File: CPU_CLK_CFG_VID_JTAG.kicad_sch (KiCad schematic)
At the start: 1 part

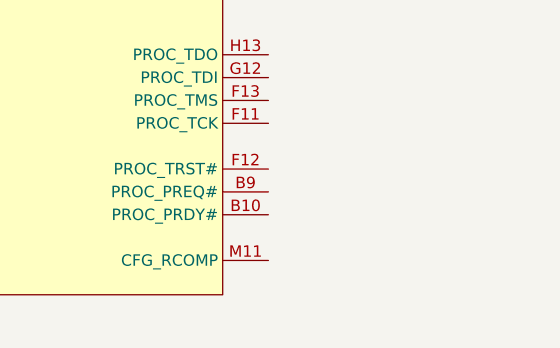
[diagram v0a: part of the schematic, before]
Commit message: partially added eDP + rearranged other display stuff
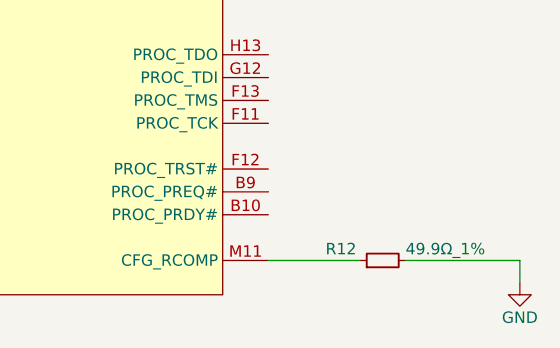
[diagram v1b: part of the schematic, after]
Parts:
- added R12: 49.9Ω_1%, Resistor_SMD:R_0402_1005Metric, symbol Device:R_Small
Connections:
- net at JCPU1.M11 (CFG_RCOMP): now also R12.1
- new net GND: R12.2
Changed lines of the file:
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@@
+	(wire
+		(pts
+			(xy 200.66 138.43) (xy 187.96 138.43)
+		)
+		(stroke
+			(width 0)
+			(type default)
+		)
+	)
 	(wire
 		(pts
@@
 	(wire
 		(pts
+			(xy 182.88 138.43) (xy 172.72 138.43)
+		)
+		(stroke
+			(width 0)
+			(type default)
+		)
+	)
+	(wire
+		(pts
+			(xy 200.66 138.43) (xy 200.66 140.97)
+		)
+		(stroke
+			(width 0)
+			(type default)
+		)
+	)
+	(wire
+		(pts
 			(xy 106.68 52.07) (xy 111.76 52.07)
 		)
@@
 			)
 		)
+	)
+	(symbol
+		(lib_id "Device:R_Small")
+		(at 185.42 138.43 90)
+		(unit 1)
+		(exclude_from_sim no)
+		(in_bom yes)
+		(on_board yes)
+		(dnp no)
+		(property "Reference" "R12"
+			(at 179.07 137.16 90)
+			(effects
+				(font
+					(size 1.27 1.27)
+				)
+				(justify right)
+			)
+		)
+		(property "Value" "49.9Ω_1%"
+			(at 187.96 137.16 90)
+			(effects
+				(font
+					(size 1.27 1.27)
+				)
+				(justify right)
+			)
+		)
+		(property "Footprint" "Resistor_SMD:R_0402_1005Metric"
+			(at 185.42 138.43 0)
+			(effects
+				(font
+					(size 1.27 1.27)
+				)
+				(hide yes)
+			)
+		)
+		(property "Datasheet" "~"
+			(at 185.42 138.43 0)
+			(effects
+				(font
+					(size 1.27 1.27)
+				)
+				(hide yes)
+			)
+		)
+		(property "Description" "Resistor, small symbol"
+			(at 185.42 138.43 0)
+			(effects
+				(font
+					(size 1.27 1.27)
+				)
+				(hide yes)
+			)
+		)
+		(pin "1"
+		)
+		(pin "2"
+		)
+		(instances
+			(project "Stroopwafel-LGA1151-CFL"
+				(path "/4bc771b8-eb19-46d0-8798-27231a7c6e83/1c68e8a0-095a-4b5e-9e5b-76592d9951b4"
+					(reference "R12")
+					(unit 1)
+				)
+			)
+		)
+	)
+	(symbol
+		(lib_id "power:GND")
+		(at 200.66 140.97 0)
+		(unit 1)
+		(exclude_from_sim no)
+		(in_bom yes)
+		(on_board yes)
+		(dnp no)
+		(property "Reference" "#PWR034"
+			(at 200.66 147.32 0)
+			(effects
+				(font
+					(size 1.27 1.27)
+				)
+				(hide yes)
+			)
+		)
+		(property "Value" "GND"
+			(at 200.66 144.78 0)
+			(effects
+				(font
+					(size 1.27 1.27)
+				)
+			)
+		)
+		(property "Footprint" ""
+			(at 200.66 140.97 0)
+			(effects
+				(font
+					(size 1.27 1.27)
+				)
+				(hide yes)
+			)
+		)
+		(property "Datasheet" ""
+			(at 200.66 140.97 0)
+			(effects
+				(font
+					(size 1.27 1.27)
+				)
+				(hide yes)
+			)
+		)
+		(property "Description" "Power symbol creates a global label with name \"GND\" , ground"
+			(at 200.66 140.97 0)
+			(effects
+				(font
+					(size 1.27 1.27)
+				)
+				(hide yes)
+			)
+		)
+		(pin "1"
+		)
+		(instances
+			(project "Stroopwafel-LGA1151-CFL"
+				(path "/4bc771b8-eb19-46d0-8798-27231a7c6e83/1c68e8a0-095a-4b5e-9e5b-76592d9951b4"
+					(reference "#PWR034")
+					(unit 1)
+				)
+			)
+		)

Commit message: Added LGA1151 socket bracket holes
stolen from another lga1151 footprint that has wrong pin numbers....
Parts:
- JCPU1: footprint A-my-stuff:LGA-1151_L47.1-W42.5-P0.91_PE115127-4041-01H -> A-my-stuff:LGA1151_TE-2287402-1
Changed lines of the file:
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@@
 			)
 		)
-		(property "Footprint" "A-my-stuff:LGA-1151_L47.1-W42.5-P0.91_PE115127-4041-01H"
+		(property "Footprint" "A-my-stuff:LGA1151_TE-2287402-1"
 			(at 142.24 246.38 0)
 			(effects

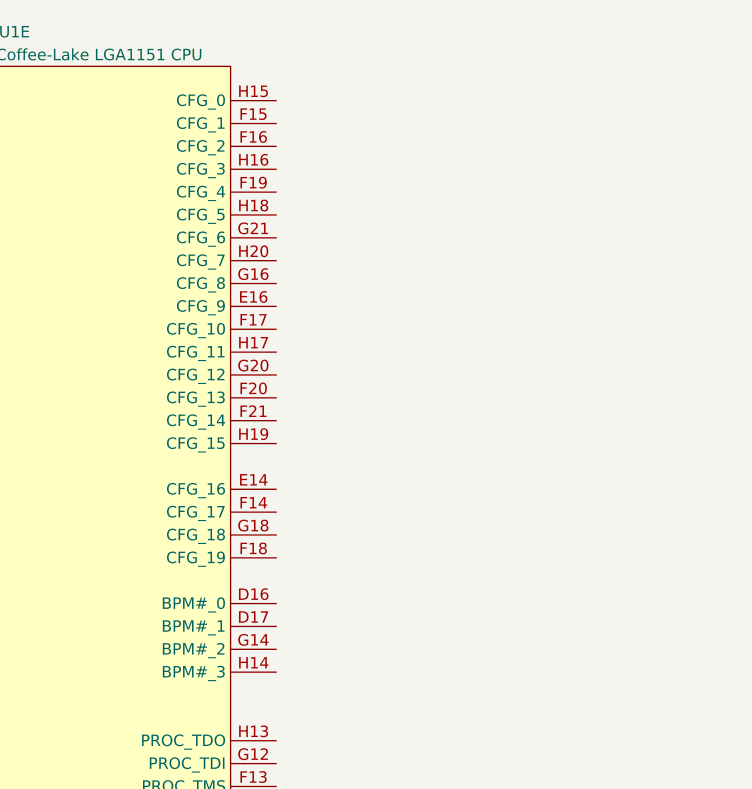
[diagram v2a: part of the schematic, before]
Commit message: Added CPU CFG resistors
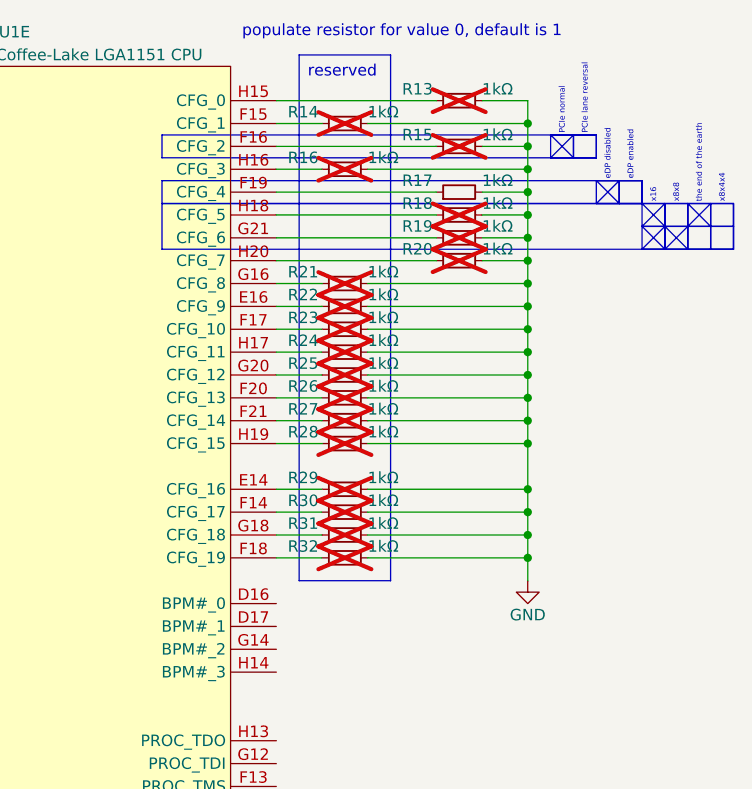
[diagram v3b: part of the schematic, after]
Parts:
- added R13, R14, R15, R16, R17, R18, R19, R20, R21, R22, R23, R24, R25, R26, R27, R28, R29, R30, R31, R32: 1kΩ, Resistor_SMD:R_0402_1005Metric, symbol Device:R_Small
- JCPU1: footprint A-my-stuff:LGA1151_TE-2287402-1 -> A-my-stuff:LGA-1151_L47.1-W42.5-P0.91_PE115127-4041-01H
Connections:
- net GND: now also R13.2, R14.2, R15.2, R16.2, R17.2, R18.2, R19.2, R20.2, R21.2, R22.2, R23.2, R24.2, R25.2, R26.2, R27.2, R28.2, R29.2, R30.2, R31.2, R32.2
- net at JCPU1.E14 (CFG_16): now also R29.1
- net at JCPU1.E16 (CFG_9): now also R22.1
- net at JCPU1.F14 (CFG_17): now also R30.1
- net at JCPU1.F15 (CFG_1): now also R14.1
- net at JCPU1.F16 (CFG_2): now also R15.1
- net at JCPU1.F17 (CFG_10): now also R23.1
- net at JCPU1.F18 (CFG_19): now also R32.1
- net at JCPU1.F19 (CFG_4): now also R17.1
- net at JCPU1.F20 (CFG_13): now also R26.1
- net at JCPU1.F21 (CFG_14): now also R27.1
- net at JCPU1.G16 (CFG_8): now also R21.1
- net at JCPU1.G18 (CFG_18): now also R31.1
- net at JCPU1.G20 (CFG_12): now also R25.1
- net at JCPU1.G21 (CFG_6): now also R19.1
- net at JCPU1.H15 (CFG_0): now also R13.1
- net at JCPU1.H16 (CFG_3): now also R16.1
- net at JCPU1.H17 (CFG_11): now also R24.1
- net at JCPU1.H18 (CFG_5): now also R18.1
- net at JCPU1.H19 (CFG_15): now also R28.1
- net at JCPU1.H20 (CFG_7): now also R20.1
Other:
- note added: "PCIe lane reversal"
- note added: "PCIe normal"
- note added: "eDP disabled"
- note added: "eDP enabled"
- note added: "populate resistor for value 0, default is 1"
- note added: "the end of the earth"
- note added: "x16"
- note added: "x8x4x4"
- note added: "x8x8"

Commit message: stroopwafel.exe
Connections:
- net CPU_24MCLK+: no longer JCPU1.K9 (CLK24P)
- net CPU_24MCLK-: no longer JCPU1.J9 (CLK24N)
- net CPU_BCLK+: no longer JCPU1.W5 (BCLKP)
- net CPU_BCLK-: no longer JCPU1.W4 (BCLKN)
- net CPU_PCIBCLK+: no longer JCPU1.W1 (PCI_BCLKP)
- net CPU_PCIBCLK-: no longer JCPU1.W2 (PCI_BCLKN)
- net at R30.1: no longer JCPU1.F14 (CFG_17)
- net at R12.1: no longer JCPU1.M11 (CFG_RCOMP)
- net at R29.1: no longer JCPU1.E14 (CFG_16)
- net at R20.1: no longer JCPU1.H20 (CFG_7)
- net at R27.1: no longer JCPU1.F21 (CFG_14)
- net at R24.1: no longer JCPU1.H17 (CFG_11)
- net at R14.1: no longer JCPU1.F15 (CFG_1)
- net at R25.1: no longer JCPU1.G20 (CFG_12)
- net at R23.1: no longer JCPU1.F17 (CFG_10)
- net at R28.1: no longer JCPU1.H19 (CFG_15)
- net at R15.1: no longer JCPU1.F16 (CFG_2)
- net at R13.1: no longer JCPU1.H15 (CFG_0)
- net at R19.1: no longer JCPU1.G21 (CFG_6)
- net at R31.1: no longer JCPU1.G18 (CFG_18)
- net at R16.1: no longer JCPU1.H16 (CFG_3)
- net at R32.1: no longer JCPU1.F18 (CFG_19)
- net at R17.1: no longer JCPU1.F19 (CFG_4)
- net at R22.1: no longer JCPU1.E16 (CFG_9)
- net at R21.1: no longer JCPU1.G16 (CFG_8)
- net at R26.1: no longer JCPU1.F20 (CFG_13)
- net at R18.1: no longer JCPU1.H18 (CFG_5)
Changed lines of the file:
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@@
 		(lib_id "A-my-stuff:Intel_CFL_1151")
 		(at 142.24 134.62 0)
-		(unit 5)
+		(unit 1)
 		(exclude_from_sim no)
 		(in_bom yes)
@@
 		(pin "J5"
 		)
-		(instances
-			(project ""
-				(path "/4bc771b8-eb19-46d0-8798-27231a7c6e83/061fe2d6-87c2-48c2-90bb-0928700512fc"
-					(reference "JCPU1")
-					(unit 5)
-				)
-				(path "/4bc771b8-eb19-46d0-8798-27231a7c6e83/1c68e8a0-095a-4b5e-9e5b-76592d9951b4"
-					(reference "JCPU1")
-					(unit 5)
-				)
-			)
-		)
 	)

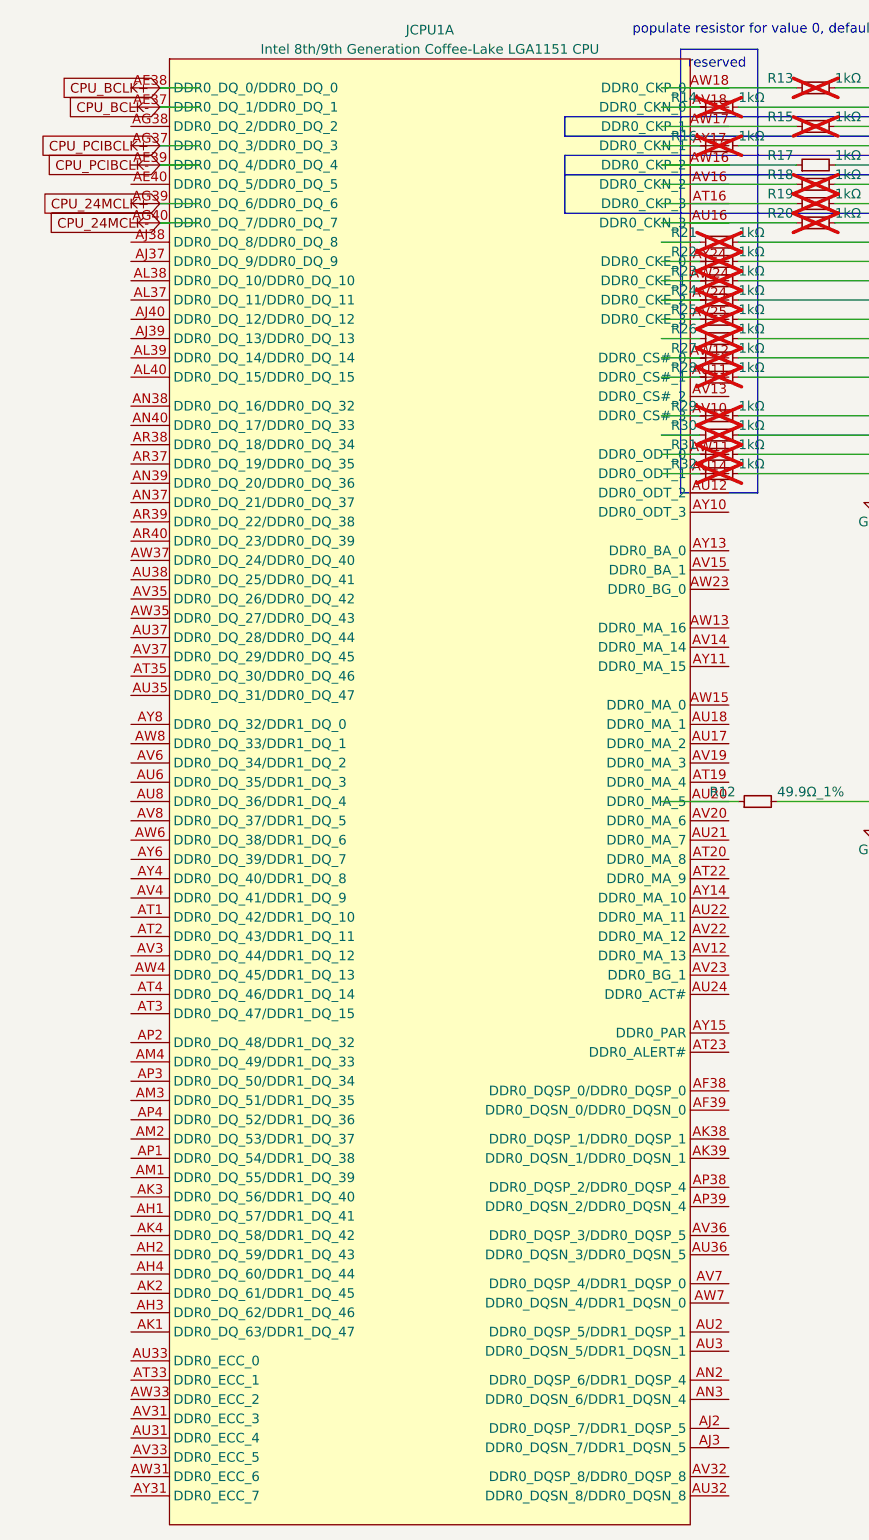
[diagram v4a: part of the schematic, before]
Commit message: Fixed entire schematic being broken
somehow every symbol with index 1 broke and updating the pcb stopped working. how does that even happen. oh well it's fixed now
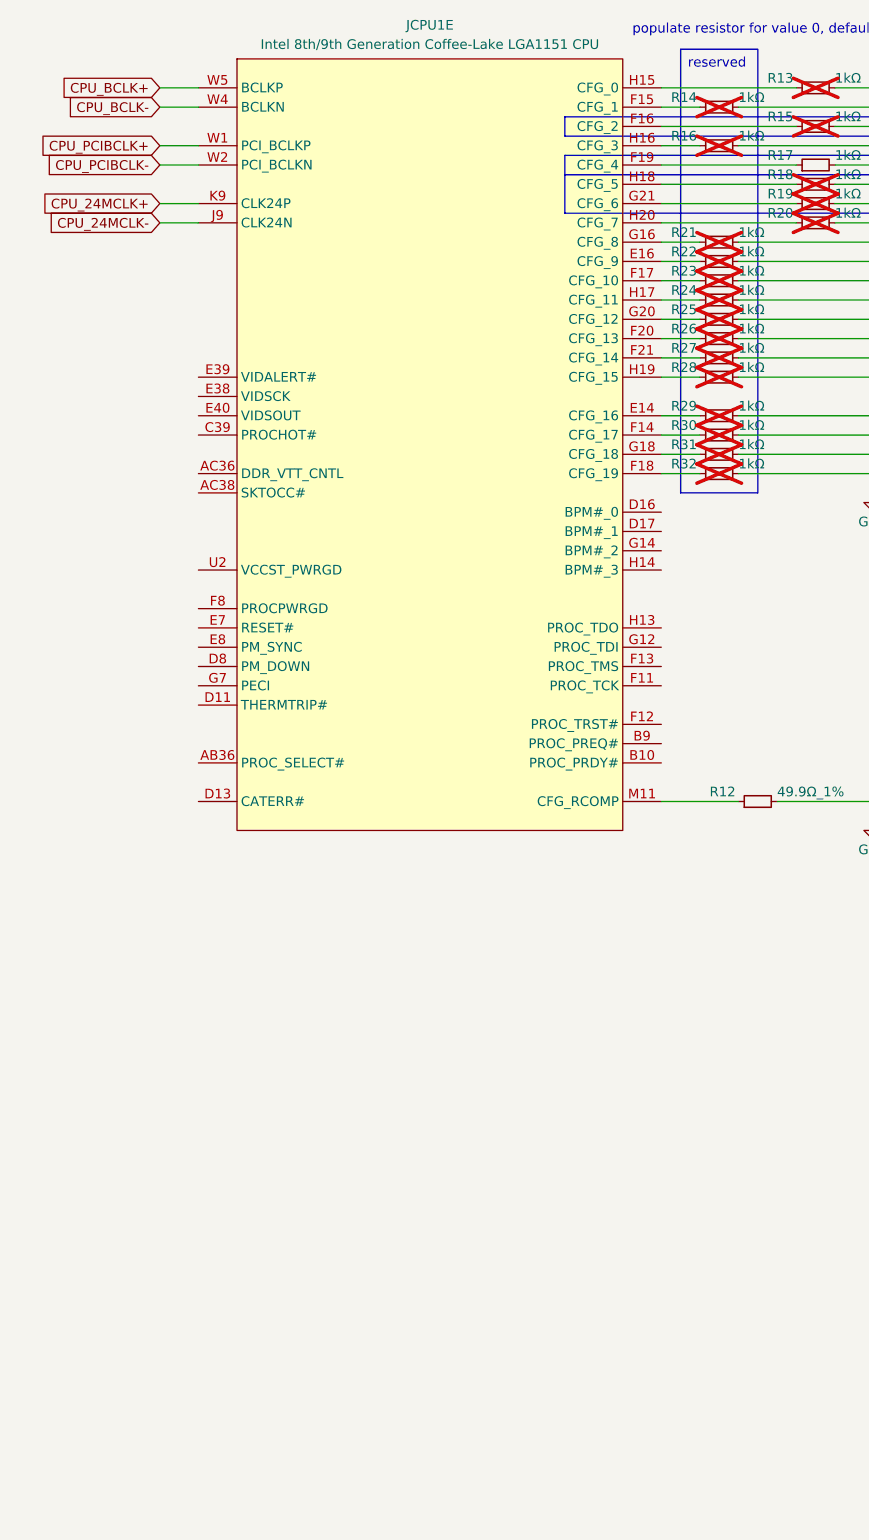
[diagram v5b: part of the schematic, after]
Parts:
- removed JCPU1: Intel 8th/9th Generation Coffee-Lake LGA1151 CPU, A-my-stuff:LGA-1151_L47.1-W42.5-P0.91_PE115127-4041-01H, symbol A-my-stuff:Intel_CFL_1151
- added JCPU1: Intel 8th/9th Generation Coffee-Lake LGA1151 CPU, A-my-stuff:LGA-1151_L47.1-W42.5-P0.91_PE115127-4041-01H, symbol A-my-stuff:Intel_CFL_1151
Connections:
- net CPU_24MCLK+: now also JCPU1.K9 (CLK24P)
- net CPU_24MCLK-: now also JCPU1.J9 (CLK24N)
- net CPU_BCLK+: now also JCPU1.W5 (BCLKP)
- net CPU_BCLK-: now also JCPU1.W4 (BCLKN)
- net CPU_PCIBCLK+: now also JCPU1.W1 (PCI_BCLKP)
- net CPU_PCIBCLK-: now also JCPU1.W2 (PCI_BCLKN)
- net at R30.1: now also JCPU1.F14 (CFG_17)
- net at R12.1: now also JCPU1.M11 (CFG_RCOMP)
- net at R29.1: now also JCPU1.E14 (CFG_16)
- net at R20.1: now also JCPU1.H20 (CFG_7)
- net at R27.1: now also JCPU1.F21 (CFG_14)
- net at R24.1: now also JCPU1.H17 (CFG_11)
- net at R14.1: now also JCPU1.F15 (CFG_1)
- net at R25.1: now also JCPU1.G20 (CFG_12)
- net at R23.1: now also JCPU1.F17 (CFG_10)
- net at R28.1: now also JCPU1.H19 (CFG_15)
- net at R15.1: now also JCPU1.F16 (CFG_2)
- net at R13.1: now also JCPU1.H15 (CFG_0)
- net at R19.1: now also JCPU1.G21 (CFG_6)
- net at R31.1: now also JCPU1.G18 (CFG_18)
- net at R16.1: now also JCPU1.H16 (CFG_3)
- net at R32.1: now also JCPU1.F18 (CFG_19)
- net at R17.1: now also JCPU1.F19 (CFG_4)
- net at R22.1: now also JCPU1.E16 (CFG_9)
- net at R21.1: now also JCPU1.G16 (CFG_8)
- net at R26.1: now also JCPU1.F20 (CFG_13)
- net at R18.1: now also JCPU1.H18 (CFG_5)

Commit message: implemented some misc cpu signals
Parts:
- added D1: Really-bad-event-led, LED_SMD:LED_0603_1608Metric, symbol Device:LED
- added Q7: MMBT3904, Package_TO_SOT_SMD:SOT-23, symbol Transistor_BJT:MMBT3904
- added R35, R36, R37: 1kΩ, Resistor_SMD:R_0402_1005Metric, symbol Device:R_Small
- added R39: 0Ω, Resistor_SMD:R_0402_1005Metric, symbol Device:R_Small
- added R40: 43Ω, Resistor_SMD:R_0402_1005Metric, symbol Device:R_Small
- added R42: 20Ω, Resistor_SMD:R_0402_1005Metric, symbol Device:R_Small
- added R43: 30Ω, Resistor_SMD:R_0402_1005Metric, symbol Device:R_Small
- added TP2: CFG-pullup-source-just-in-case, TestPoint:TestPoint_Pad_D2.0mm, symbol Connector:TestPoint
- added TP3: PROC_SELECT#, TestPoint:TestPoint_Pad_D2.0mm, symbol Connector:TestPoint
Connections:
- net GND: now also D1.1 (K), Q7.2 (E)
- net at JCPU1.AB36 (PROC_SELECT#): now also TP3.1
- net THERMTRIP#: now reaches JCPU1.D11 (THERMTRIP#)
- net THERMTRIP#: now also R37.1
- net CATERR#: now reaches JCPU1.D13 (CATERR#)
- net CATERR#: now also Q7.1 (B), R35.1
- net at JCPU1.D8 (PM_DOWN): now also R42.2
- net PLTRST_CPU#: now reaches JCPU1.E7 (RESET#)
- net at JCPU1.E8 (PM_SYNC): now also R43.2
- net at JCPU1.G7 (PECI): now also R39.2, R40.2
- new net: D1.2 (A), Q7.3 (C), R36.1
- new net PECI_EC: R40.1
- new net PECI_PCH: R39.1
- new net PM_DOWN_PCH: R42.1
- new net PM_SYNC_PCH: R43.1
- new net VCCIO: TP2.1
- new net VCCST: R35.2, R37.2
- new net temp_3.3V: R36.2
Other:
- note added: "check transistor part"
- moved on the sheet: JCPU1E, R12, R13, R14, R15, R16, R17, R18, R19, R20, R21, R22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

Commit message: idek what i changed anymore but there's a bunch of new stuff lol
iirc i did some more misc cpu pins and a bunch of pch pcie stuff
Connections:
- net CPU_DDR_VTT_CNTL: now reaches JCPU1.AC36 (DDR_VTT_CNTL)
- net CPU_PWRGD: now reaches JCPU1.F8 (PROCPWRGD)
- net CPU_VCCST_PWRGD: now reaches JCPU1.U2 (VCCST_PWRGD)
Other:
- note added: "meow"
- moved on the sheet: R37, R39, R40, R42, R43, TP3

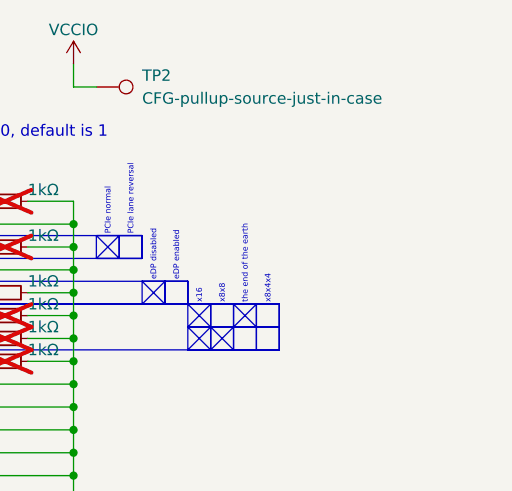
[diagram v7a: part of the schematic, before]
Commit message: Restructured schematic
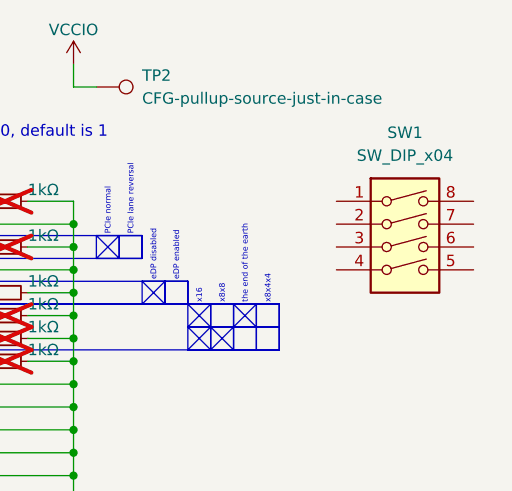
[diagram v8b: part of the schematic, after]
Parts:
- added SW1: SW_DIP_x04, symbol Switch:SW_DIP_x04
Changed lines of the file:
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@@
+	)
+	(symbol
+		(lib_id "Switch:SW_DIP_x04")
+		(at 271.78 49.53 0)
+		(unit 1)
+		(exclude_from_sim no)
+		(in_bom yes)
+		(on_board yes)
+		(dnp no)
+		(fields_autoplaced yes)
+		(property "Reference" "SW1"
+			(at 271.78 36.83 0)
+			(effects
+				(font
+					(size 1.27 1.27)
+				)
+			)
+		)
+		(property "Value" "SW_DIP_x04"
+			(at 271.78 39.37 0)
+			(effects
+				(font
+					(size 1.27 1.27)
+				)
+			)
+		)
+		(property "Footprint" ""
+			(at 271.78 49.53 0)
+			(effects
+				(font
+					(size 1.27 1.27)
+				)
+				(hide yes)
+			)
+		)
+		(property "Datasheet" "~"
+			(at 271.78 49.53 0)
+			(effects
+				(font
+					(size 1.27 1.27)
+				)
+				(hide yes)
+			)
+		)
+		(property "Description" "4x DIP Switch, Single Pole Single Throw (SPST) switch, small symbol"
+			(at 271.78 49.53 0)
+			(effects
+				(font
+					(size 1.27 1.27)
+				)
+				(hide yes)
+			)
+		)
+		(pin "2"
+		)
+		(pin "3"
+		)
+		(pin "7"
+		)
+		(pin "5"
+		)
+		(pin "8"
+		)
+		(pin "1"
+		)
+		(pin "6"
+		)
+		(pin "4"
+		)
+		(instances
+			(project ""
+				(path "/4bc771b8-eb19-46d0-8798-27231a7c6e83/1c68e8a0-095a-4b5e-9e5b-76592d9951b4"
+					(reference "SW1")
+					(unit 1)
+				)
+			)
+		)
 	)
 	(symbol
